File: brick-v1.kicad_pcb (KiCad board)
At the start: 2 copper layers, 76.2 x 62.2 mm, 15 parts, among them J1 battery_header, U1 XBEE S2C PRO, U2 esp32, U3 L7805, U4 ULTRASONIC SENSOR, U5 Teensy4.1

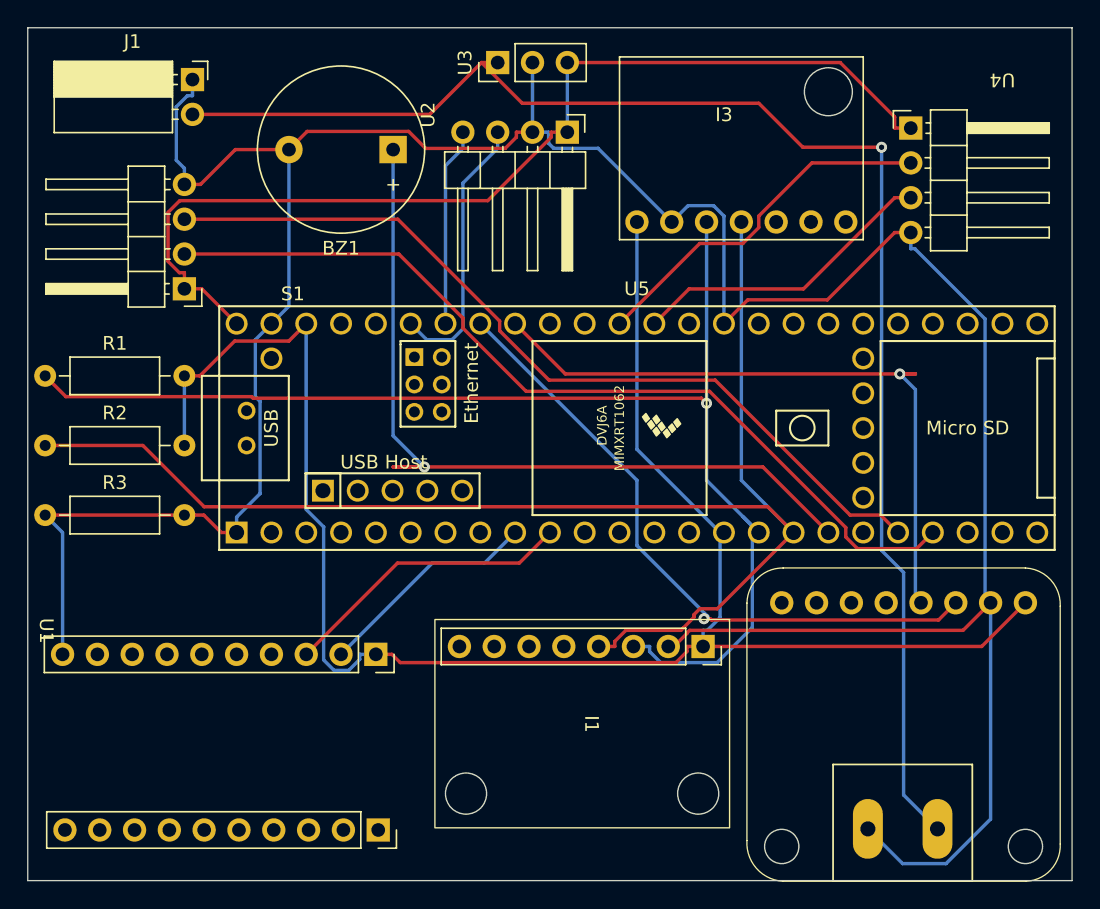
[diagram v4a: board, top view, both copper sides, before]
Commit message: fixed ina260 traces
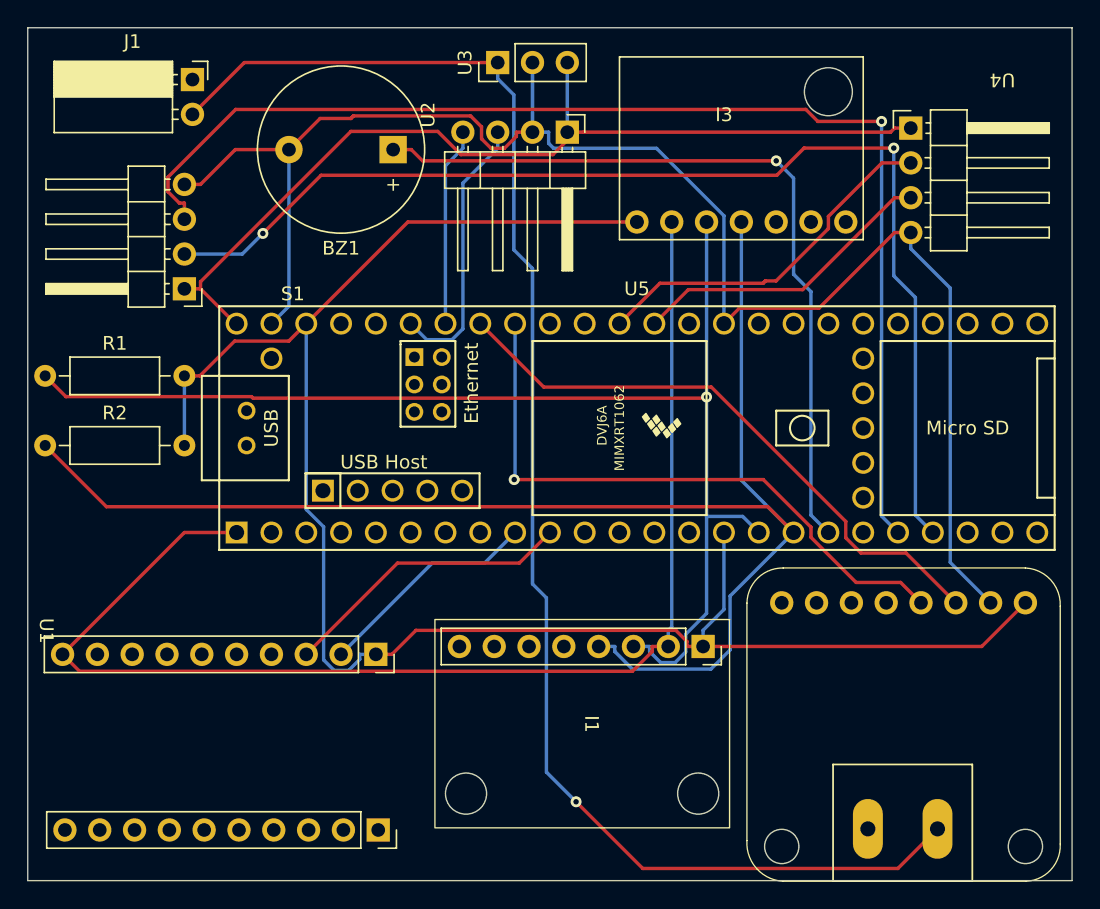
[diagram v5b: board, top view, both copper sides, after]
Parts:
- removed R3: R-Device, Resistor_THT:R_Axial_DIN0207_L6.3mm_D2.5mm_P10.16mm_Horizontal
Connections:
- I1 pad 2: GND -> T_GND
- I2 pad 2: GND -> unconnected-(I2-VIN--Pad2)
- I3 pad 2: GND -> T_GND
- J1 pad 1: GND -> unconnected-(J1-Pin_1-Pad1)
- U1 pad 10: GND -> T_GND
- U5 pad GND2: GND -> T_GND
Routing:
- net GND: track 220.7 -> 118.9 mm
- net T_GND: track 0.00 -> 93.1 mm
- net RX7: track 62.0 -> 88.8 mm, vias 0 -> 1
- net TX7: track 64.8 -> 84.2 mm, vias 0 -> 2
- net Net-(BZ1--): track 64.7 -> 57.0 mm
- net VCC: track 75.5 -> 68.9 mm
- net SDA: track 51.5 -> 45.2 mm
- net SCL: track 47.6 -> 43.8 mm, vias 1 -> 0
- net SDA2: track 99.7 -> 103.0 mm
- net /V+: track 107.0 -> 109.7 mm
- net T_VCC: track 129.6 -> 131.7 mm
- net SCL2: track 92.1 -> 90.1 mm

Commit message: changed pcb size and sensor placements
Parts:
- added G***: LOGO, rrc_logo:tmu, F.Cu at (204.3, 112.2)
- added U6: ESC, RRC_footprint:BLHeLi_esc, F.Cu at (262.2, 102.5)
- added U7: ESC, RRC_footprint:BLHeLi_esc, F.Cu at (256.9, 56.6)
- added U8: ULTRASONIC SENSOR, rrc_bn220_gps:BN220, F.Cu at (216.3, 79.3)
- added U9: Teensy4.1, rrc_teensy:Teensy41, F.Cu at (223.5, 82.5)
- U2: value esp32 -> ESC; footprint rrc_bn220_gps:BN220 -> RRC_footprint:BLHeLi_esc
- U3: value L7805 -> ESC; footprint Connector_PinHeader_2.54mm:PinHeader_1x03_P2.54mm_Vertical -> RRC_footprint:BLHeLi_esc
- U4: value ULTRASONIC SENSOR -> esp32
- U5: value Teensy4.1 -> L7805; footprint rrc_teensy:Teensy41 -> Connector_PinHeader_2.54mm:PinHeader_1x03_P2.54mm_Vertical
- moved Logo1 201.4 mm to (15.1, 6.10)
- moved J1 96.7 mm to (245.0, 120.5), turned to 90 degrees
- moved U1 92.7 mm to (253.4, 92.2), turned to 180 degrees
- moved U3 90.9 mm to (262.3, 116.2)
- moved R1 88.7 mm to (247.7, 98.8), turned to -90 degrees
- moved R2 83.4 mm to (243.4, 98.8), turned to -90 degrees
- moved U5 68.1 mm to (259.1, 123.2)
- moved U2 65.1 mm to (223.6, 130.5)
- moved BZ1 62.9 mm to (200.3, 123.7), turned to 0 degrees
- moved S1 49.6 mm to (198.6, 79.2), turned to 90 degrees
- moved U4 37.0 mm to (243.7, 112.5), turned to -90 degrees
- moved I3 35.6 mm to (244.7, 57.0), turned to 180 degrees
- moved I1 26.0 mm to (226.3, 99.5), turned to 90 degrees
- moved I2 20.3 mm to (203.6, 102.7)
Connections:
- I2 pad 1: /V+ -> Vs
- I2 pad 4: GND -> T_GND
- I2 pad 5: SCL -> SCL2
- I2 pad 6: SDA -> SDA2
- J1 pad 1: unconnected-(J1-Pin_1-Pad1) -> GND
- J1 pad 2: /V+ -> Vs
- U2 pad 1: VCC -> Vs
- U2 pad 3: RX5 -> T_GND
- U2 pad 4: TX5 -> A13
- U3 pad 1: /V+ -> Vs
- U3 pad 3: VCC -> T_GND
- U4 pad 2: A1 -> GND
- U4 pad 3: A0 -> RX5
- U4 pad 4: GND -> TX5
- U5 pad 1: unconnected-(U5-1_TX1_CTX2_MISO1-Pad1) -> Vs
- U5 pad 2: unconnected-(U5-2_OUT2-Pad2) -> GND
- U5 pad 3: unconnected-(U5-3_LRCLK2-Pad3) -> VCC
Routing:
- net Vs: track 0.00 -> 127.1 mm
- net /V+: track 109.7 -> 0.00 mm, vias 1 -> 0
- net VCC: track 68.9 -> 164.9 mm, vias 0 -> 1
- net GND: track 118.9 -> 195.4 mm, vias 0 -> 1
- net T_GND: track 93.1 -> 159.8 mm
- net A9: track 0.00 -> 63.9 mm
- net A8: track 0.00 -> 58.2 mm
- net TX5: track 14.5 -> 67.1 mm
- net RX5: track 20.0 -> 66.9 mm
- net SDA: track 45.2 -> 0.00 mm, vias 1 -> 0
- net A13: track 0.00 -> 44.1 mm, vias 0 -> 1
- net SCL: track 43.8 -> 0.00 mm
- net RX2: track 16.4 -> 55.9 mm, vias 0 -> 1
- net TX2: track 21.5 -> 60.4 mm, vias 0 -> 1
- net A10: track 0.00 -> 32.8 mm
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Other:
- board size 76.2 x 62.2 mm -> 74.2 x 74.2 mm

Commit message: AC_flight controller updated v1.5
-made 4 layer board
-added esp32 camera
-removed buzzer
-reduced area of pcb
-added TMU logos and my name and other descriptors
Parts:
- removed BZ1: Buzzer-Device, Buzzer_Beeper:Buzzer_12x9.5RM7.6
- removed G***: LOGO, rrc_logo:tmu
- I2: moved to B.Cu
- Logo1: footprint rrc_logo:tmu -> rrc_logo:picturae; moved to B.Cu
- S1, U8: footprint rrc_bn220_gps:BN220 -> Connector_PinSocket_2.54mm:PinSocket_1x04_P2.54mm_Vertical
- U4: footprint rrc_bn220_gps:BN220 -> thesis_lib:esp32_cam
- moved Logo1 262.0 mm to (258.2, 103.8)
- moved U7 88.8 mm to (191.0, 116.0), turned to 0 degrees
- moved J1 72.0 mm to (204.2, 61.2)
- moved U6 71.4 mm to (191.0, 107.2), turned to 0 degrees
- moved I2 60.8 mm to (254.1, 68.7)
- moved R1 47.2 mm to (211.5, 68.6), turned to 0 degrees
- moved U3 44.2 mm to (221.3, 132.8)
- moved U8 43.8 mm to (229.6, 121.1)
- moved U4 39.1 mm to (205.7, 121.7), turned to 0 degrees
- moved S1 34.9 mm to (227.8, 98.3)
- moved U1 33.1 mm to (265.7, 122.9), turned to 90 degrees
- moved I1 33.1 mm to (219.8, 67.0), turned to -90 degrees
- moved R2 26.3 mm to (236.1, 73.4), turned to 90 degrees
- moved U5 24.3 mm to (237.1, 112.9), turned to 180 degrees
- moved I3 20.0 mm to (228.2, 68.4), turned to -90 degrees
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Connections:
- I1 pad 3: SCL2 -> SCL
- I1 pad 4: SDA2 -> SDA
- I2 pad 5: SCL2 -> SCL
- I2 pad 6: SDA2 -> SDA
- I3 pad 3: SCL2 -> SCL
- I3 pad 4: SDA2 -> SDA
- R1 pad 1: SCL2 -> SCL
- R2 pad 1: SDA2 -> SDA
- S1 pad 2: TX7 -> TX5
- S1 pad 3: RX7 -> RX5
- U4 pad 3: RX5 -> unconnected-(U4-TX-Pad3)
- U4 pad 4: TX5 -> unconnected-(U4-RX-Pad4)
- U9 pad 26: Net-(BZ1--) -> unconnected-(U9-26_A12_MOSI1-Pad26)
- U9 pad 28: RX7 -> unconnected-(U9-28_RX7-Pad28)
- U9 pad 29: TX7 -> unconnected-(U9-29_TX7-Pad29)
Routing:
- net SCL2: track 96.8 -> 0.00 mm
- net SDA2: track 87.5 -> 0.00 mm, vias 1 -> 0
- net VCC: track 164.9 -> 82.7 mm, vias 1 -> 0
- net SDA: track 0.00 -> 76.0 mm
- net A1: track 22.3 -> 91.6 mm
- net Net-(BZ1--): track 65.3 -> 0.00 mm, vias 1 -> 0
- net TX7: track 63.3 -> 0.00 mm, vias 1 -> 0
- net RX7: track 58.9 -> 0.00 mm, vias 1 -> 0
- net A0: track 19.4 -> 76.8 mm
- net SCL: track 0.00 -> 47.9 mm
- net GND: track 195.4 -> 241.1 mm, vias 1 -> 0
- net A9: track 63.9 -> 30.9 mm
- net T_GND: track 159.8 -> 190.2 mm
- net A10: track 32.8 -> 61.0 mm
- net TX2: track 60.4 -> 35.5 mm, vias 1 -> 0
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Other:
- board size 74.2 x 74.2 mm -> 64 x 64.7 mm
- copper layers 2 -> 4
- board text added: "By Alessandro Ciniello MASc Thesis 11/17/2025"
- board text added: "flight controller v1.5"

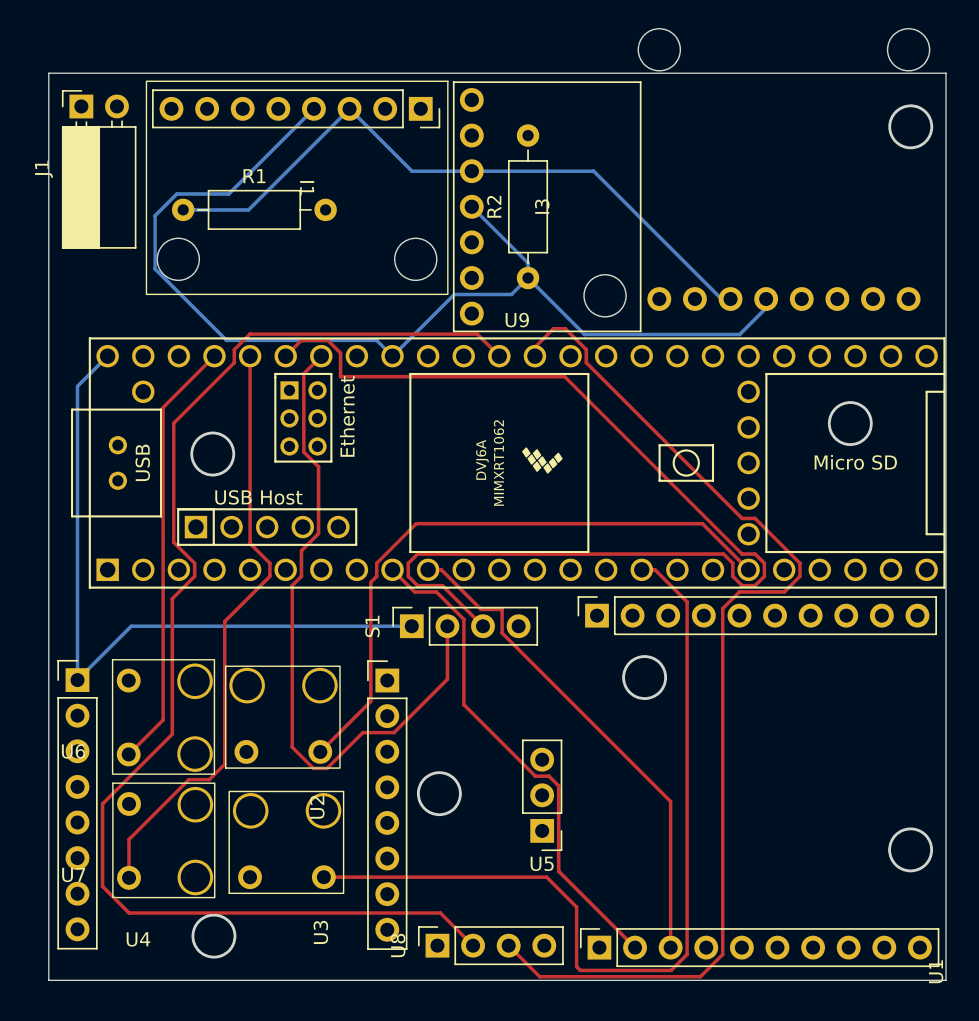
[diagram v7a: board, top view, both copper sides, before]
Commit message: deleted and organized footprints
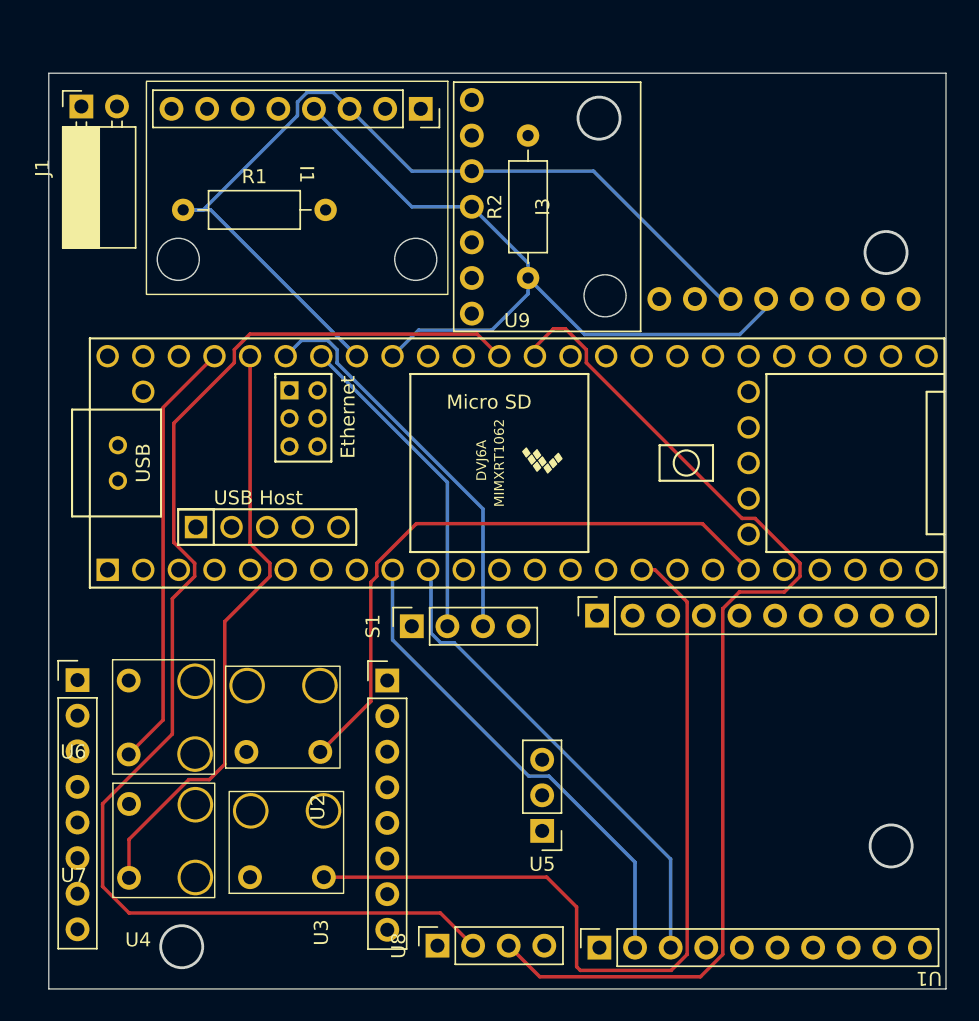
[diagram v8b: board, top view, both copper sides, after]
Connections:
- I1 pad 2: T_GND -> GND
- I2 pad 4: T_GND -> GND
- I3 pad 2: T_GND -> GND
- U1 pad 10: T_GND -> GND
- U2 pad 3: T_GND -> GND
- U3 pad 3: T_GND -> GND
- U6 pad 3: T_GND -> GND
- U7 pad 3: T_GND -> GND
- U9 pad GND2: T_GND -> GND
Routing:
- net T_GND: track 190.2 -> 0.00 mm
- net RX5: track 78.3 -> 28.4 mm
- net VCC: track 82.7 -> 128.1 mm
- net GND: track 241.1 -> 211.4 mm
- net TX5: track 47.7 -> 23.0 mm
- net SDA: track 76.0 -> 53.0 mm
- net SCL: track 47.9 -> 66.2 mm
- net TX2: track 35.5 -> 34.7 mm
- net RX2: track 35.6 -> 35.0 mm
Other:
- board size 64 x 64.7 mm -> 64 x 65.3 mm
- board text added: "By Alessandro Ciniello MASc Thesis 01/17/2026"
- board text added: "flight controller v1.6"
- board text removed: "By Alessandro Ciniello MASc Thesis 11/17/2025"
- board text removed: "flight controller v1.5"
